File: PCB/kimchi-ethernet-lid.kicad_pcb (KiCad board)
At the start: 4 copper layers, 65 x 32 mm, 8 parts, among them J1 DF40HC(3.5)-60DS, J2 DF40HC(3.5)-60DS, U1 24C32

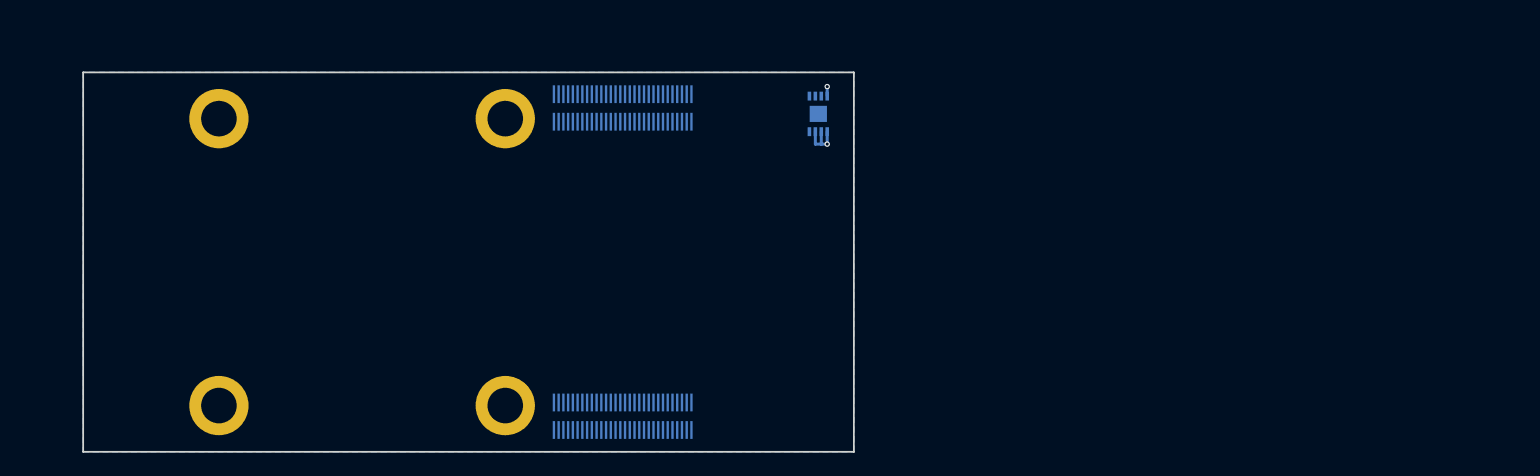
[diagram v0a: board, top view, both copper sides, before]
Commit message: Libraries, Schematic Capture, Part Placement, Lauout
Created and added all realted components. Completed schematic capture. Part placement all bu down, layout in progress since schematic capture.

Had to change out mag jacks a lot to find one that would fit the design
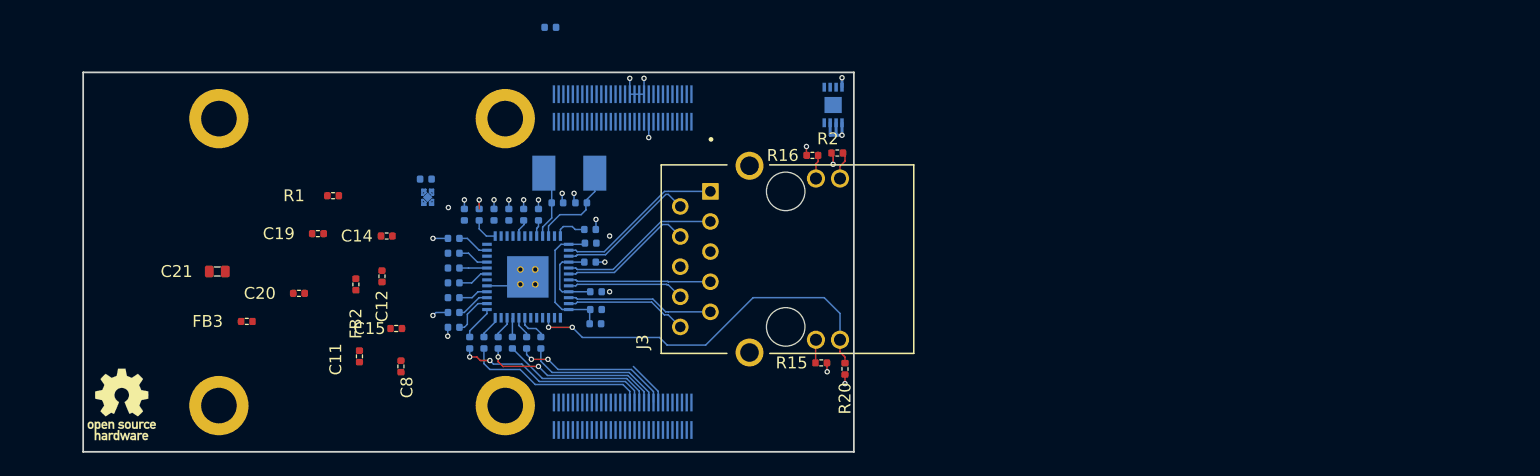
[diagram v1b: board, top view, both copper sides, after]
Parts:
- added C1: C0402C104K9PACTU, AVR-KiCAD-Lib-Resistors:R0402, B.Cu at (150.2, 112.5)
- added C10: C0402C104K9PACTU, AVR-KiCAD-Lib-Resistors:R0402, B.Cu at (142.9, 106.0)
- added C11: C0402C104K9PACTU, AVR-KiCAD-Lib-Resistors:R0402, F.Cu at (130.3, 118.0)
- added C12: C0402C104K9PACTU, AVR-KiCAD-Lib-Resistors:R0402, F.Cu at (132.2, 111.2)
- added C13: C0402C104K9PACTU, AVR-KiCAD-Lib-Resistors:R0402, B.Cu at (138.2, 115.5)
- added C14: C0402C104K9PACTU, AVR-KiCAD-Lib-Resistors:R0402, F.Cu at (132.6, 107.8)
- added C15: 0402ZD105KAT2A, AVR-KiCAD-Lib-Resistors:R0402, F.Cu at (133.4, 115.6)
- added C16: GRM155R61A475MEAAD, kimchi_ulid:C0402, B.Cu at (145.4, 106.0)
- added C17: 04025A180GAT2A, kimchi_ulid:C0402, B.Cu at (149.0, 105.0)
- added C18: 04025A180GAT2A, kimchi_ulid:C0402, B.Cu at (147.0, 105.0)
- added C19: C0402C104K9PACTU, AVR-KiCAD-Lib-Resistors:R0402, F.Cu at (126.8, 107.6)
- added C2: C0402C104K9PACTU, AVR-KiCAD-Lib-Resistors:R0402, B.Cu at (149.8, 110.0)
- added C20: C0402C104K9PACTU, AVR-KiCAD-Lib-Resistors:R0402, F.Cu at (125.2, 112.6)
- added C21: C0603C103KARACAUTO, kimchi_ulid:C0603, F.Cu at (118.3, 110.8)
- added C3: C0402C104K9PACTU, AVR-KiCAD-Lib-Resistors:R0402, B.Cu at (150.2, 114.0)
- added C4: C0402C104K9PACTU, AVR-KiCAD-Lib-Resistors:R0402, B.Cu at (149.8, 108.4)
- added C5: C0402C104K9PACTU, AVR-KiCAD-Lib-Resistors:R0402, B.Cu at (146.4, 90.2)
- added C6: C0402C104K9PACTU, AVR-KiCAD-Lib-Resistors:R0402, B.Cu at (139.2, 106.0)
- added C7: C0402C104K9PACTU, AVR-KiCAD-Lib-Resistors:R0402, B.Cu at (141.7, 106.0)
- added C8: C0402C104K9PACTU, AVR-KiCAD-Lib-Resistors:R0402, F.Cu at (133.8, 118.8)
- added C9: 0402ZD105KAT2A, AVR-KiCAD-Lib-Resistors:R0402, B.Cu at (135.9, 103.0)
- added FB1: MMZ1005S601CTD25, kimchi_ulid:R0402, B.Cu at (150.2, 115.2)
- added FB2: MMZ1005S601CTD25, kimchi_ulid:R0402, F.Cu at (130.0, 111.9)
- added FB3: MMZ1005S601CTD25, kimchi_ulid:R0402, F.Cu at (120.8, 115.0)
- added J3: ARJM11C7-502-AB-ER2-T, kimchi_ulid:ABRACON_ARJM11C7-502-AB-ER2-T, F.Cu at (166.2, 109.8)
- added R1: RC0402FR-071KL, kimchi_ulid:R0402, F.Cu at (128.1, 104.4)
- added R10: RC0402FR-0722RL, kimchi_ulid:R0402, B.Cu at (138.2, 111.8)
- added R11: RC0402FR-0722RL, kimchi_ulid:R0402, B.Cu at (138.2, 113.0)
- added R12: RC0402FR-0722RL, kimchi_ulid:R0402, B.Cu at (138.2, 114.2)
- added R13: RC0402FR-074K7L, kimchi_ulid:R0402, B.Cu at (140.4, 106.0)
- added R15: RC0402FR-071KL, kimchi_ulid:R0402, F.Cu at (169.2, 118.5)
- added R16: RC0402FR-071KL, kimchi_ulid:R0402, F.Cu at (168.5, 101.0)
- added R17: RC0402FR-0710KL, kimchi_ulid:R0402, B.Cu at (144.2, 106.0)
- added R18: RMCF0402FT12K1, kimchi_ulid:R0402, B.Cu at (149.8, 107.2)
- added R2: RC0402FR-071KL, kimchi_ulid:R0402, F.Cu at (170.6, 100.8)
- added R20: RC0402FR-071KL, kimchi_ulid:R0402, F.Cu at (171.2, 119.0)
- added R21: RC0402FR-0722RL, kimchi_ulid:R0402, B.Cu at (140.8, 116.8)
- added R22: RC0402FR-0722RL, kimchi_ulid:R0402, B.Cu at (139.6, 116.8)
- added R23: RC0402FR-0722RL, kimchi_ulid:R0402, B.Cu at (145.6, 116.8)
- added R24: RC0402FR-0722RL, kimchi_ulid:R0402, B.Cu at (144.4, 116.8)
- added R25: RC0402FR-0722RL, kimchi_ulid:R0402, B.Cu at (143.2, 116.8)
- added R26: RC0402FR-0722RL, kimchi_ulid:R0402, B.Cu at (142.0, 116.8)
- added R7: RC0402FR-0722RL, kimchi_ulid:R0402, B.Cu at (138.2, 108.0)
- added R8: RC0402FR-0722RL, kimchi_ulid:R0402, B.Cu at (138.2, 109.2)
- added R9: RC0402FR-0722RL, kimchi_ulid:R0402, B.Cu at (138.2, 110.5)
- added U3: KSZ9031RNXCC, kimchi_ulid:QFN50P700X700X90-49N, B.Cu at (144.5, 111.2)
- added U4: TLV73312PDQNR3, kimchi_ulid:TLV73312PDQNR3, B.Cu at (136.1, 104.5)
- added Y1: ABM3-25.000MHZ-D2Y-T, kimchi_ulid:XTAL500X320X130N, B.Cu at (148.0, 102.5)
- H1, H2, H3, H4: value MountingHole_Pad -> Mechanical_MountingHole_Pad
- LOGO1: value Logo_Open_Hardware_Small -> Graphic_Logo_Open_Hardware_Small; footprint Symbol:OSHW-Logo_5.7x6mm_SilkScreen -> kimchi_ulid:OSHW-Logo_5.7x6mm_SilkScreen; moved to F.Cu
- moved U1 1.46 mm to (170.2, 96.8)
- moved LOGO1 1.25 mm to (110.2, 122.0), turned to 0 degrees
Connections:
- J1 pad 1: (no net) -> /USDHC3_CMD
- J1 pad 17: (no net) -> I2C3_SDA
- J1 pad 18: (no net) -> I2C3_SCL
- J1 pad 19: (no net) -> I2C2_SDA
- J1 pad 2: (no net) -> /USDHC3_CLK
- J1 pad 20: (no net) -> I2C2_SCL
- J1 pad 21: (no net) -> I2C1_SDA
- J1 pad 22: (no net) -> I2C1_SCL
- J1 pad 23: (no net) -> ECSPI1_SCLK
- J1 pad 24: (no net) -> ECSPI1_SS0
- J1 pad 25: (no net) -> ECSPI1_MOSI
- J1 pad 26: (no net) -> ECSPI1_MISO
- J1 pad 27: (no net) -> ECSPI2_SCLK
- J1 pad 28: (no net) -> ECSPI2_SS0
- J1 pad 29: (no net) -> ECSPI2_MOSI
- J1 pad 3: (no net) -> /USDHC3_DATA3
- J1 pad 30: (no net) -> ECSPI2_MISO
- J1 pad 31: (no net) -> /DISP_D0_N
- J1 pad 32: (no net) -> /DISP_D0_P
- J1 pad 33: (no net) -> /DISP_D1_N
- J1 pad 34: (no net) -> /DISP_D1_P
- J1 pad 35: (no net) -> /DISP_CK_N
- J1 pad 36: (no net) -> /DISP_CK_P
- J1 pad 37: (no net) -> /DISP_D2_N
- J1 pad 38: (no net) -> /DISP_D2_P
- J1 pad 39: (no net) -> /DISP_D3_N
- J1 pad 4: (no net) -> /USDHC3_DATA0
- J1 pad 40: (no net) -> /DISP_D3_P
- J1 pad 41: (no net) -> /CAM_D0_N
- J1 pad 42: (no net) -> /CAM_D0_P
- J1 pad 43: (no net) -> /CAM_D1_N
- J1 pad 44: (no net) -> /CAM_D1_P
- J1 pad 45: (no net) -> /CAM_CK_N
- J1 pad 46: (no net) -> /CAM_CK_P
- J1 pad 47: (no net) -> /CAM_D2_N
- J1 pad 48: (no net) -> /CAM_D2_P
- J1 pad 49: (no net) -> /CAM_D3_N
- J1 pad 5: (no net) -> /USDHC3_DATA1
- J1 pad 50: (no net) -> /CAM_D3_P
- J1 pad 52: (no net) -> UIM_VPP
- J1 pad 53: (no net) -> UIM_RESET_N
- J1 pad 54: (no net) -> UIM_CLK
- J1 pad 55: (no net) -> UIM_DATA
- J1 pad 56: (no net) -> UIM_PWR
- J1 pad 57: (no net) -> USB2_VBUS
- J1 pad 58: (no net) -> USB2_ID
- J1 pad 59: (no net) -> USB2_DN
- J1 pad 6: (no net) -> /USDHC3_DATA2
- J1 pad 60: (no net) -> USB2_DP
- J2 pad 1: (no net) -> /ENET_MDIO
- J2 pad 10: (no net) -> /ENET_TD0
- J2 pad 11: (no net) -> /ENET_TD3
- J2 pad 12: (no net) -> /ENET_TD2
- J2 pad 13: (no net) -> /ENET_TX_CTL
- J2 pad 14: (no net) -> /ENET_TXC
- J2 pad 15: (no net) -> SAI2_RXD0
- J2 pad 16: (no net) -> SAI2_TXFS
- J2 pad 17: (no net) -> SAI2_RXC
- J2 pad 18: (no net) -> SAI2_TXD0
- J2 pad 19: (no net) -> SAI2_TXC
- J2 pad 2: (no net) -> /ENET_MDC
- J2 pad 20: (no net) -> SAI2_MCLK
- J2 pad 21: (no net) -> SAI2_RXFS
- J2 pad 22: (no net) -> GPIO1[15]
- J2 pad 23: (no net) -> GPIO1[14]
- J2 pad 24: (no net) -> GPIO1[13]
- J2 pad 25: (no net) -> GPIO1[12]
- J2 pad 26: (no net) -> GPIO1[11]
- J2 pad 27: (no net) -> GPIO1[10]
- J2 pad 28: (no net) -> GPIO1[9]
- J2 pad 29: (no net) -> GPIO1[1]
- J2 pad 3: (no net) -> /ENET_RD3
- J2 pad 30: (no net) -> GPIO1[0]
- J2 pad 31: (no net) -> SAI3_TXC
- J2 pad 32: (no net) -> SAI3_TXD
- J2 pad 33: (no net) -> SAI3_RXD
- J2 pad 34: (no net) -> SAI3_RXFS
- J2 pad 35: (no net) -> SAI3_RXC
- J2 pad 36: (no net) -> SAI3_TXFS
- J2 pad 37: (no net) -> SAI3_MCLK
- J2 pad 4: (no net) -> /ENET_RD1
- J2 pad 46: (no net) -> UART1_TX
- J2 pad 47: (no net) -> UART1_RX
- J2 pad 48: (no net) -> UART3_TX
- J2 pad 49: (no net) -> UART3_RX
- J2 pad 5: (no net) -> /ENET_RD2
- J2 pad 58: (no net) -> Net-(J2-Pad58)
- J2 pad 59: (no net) -> PCIE_USB_D_P
- J2 pad 6: (no net) -> /ENET_RD0
- J2 pad 60: (no net) -> PCIE_USB_D_N
- J2 pad 7: (no net) -> /ENET_RXC
- J2 pad 8: (no net) -> /ENET_RX_CTL
- J2 pad 9: (no net) -> /ENET_TD1
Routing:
- net /LED2: track 0.00 -> 32.6 mm, vias 0 -> 2
- net GND: track 0.00 -> 17.8 mm, vias 0 -> 16
- net /ENET_TX_CTL: track 0.00 -> 16.8 mm, vias 0 -> 2
- net /ENET_TXC: track 0.00 -> 15.5 mm
- net /ENET_TD3: track 0.00 -> 15.4 mm, vias 0 -> 2
- net /TRD1+: track 0.00 -> 14.1 mm
- net /TRD2+: track 0.00 -> 13.7 mm
- net /ENET_TD1: track 0.00 -> 13.4 mm, vias 0 -> 2
- net /ENET_TD2: track 0.00 -> 13.1 mm
- net /TRD4+: track 0.00 -> 12.4 mm
- net /ENET_TD0: track 0.00 -> 12.1 mm
- net /TRD3+: track 0.00 -> 12.0 mm
- net /TRD1-: track 0.00 -> 12.0 mm
- net Net-(C3-Pad1): track 0.00 -> 11.6 mm
- net /TRD2-: track 0.00 -> 11.6 mm
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- added copper zone on In2.Cu, net VDD_PHY_1V2
- removed copper zone on B.Cu, net GND
- removed copper zone on In2.Cu, net VDD_3V3

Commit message: Change in design
Swapped orientation of PHY and position of ethernet connector, moving computers
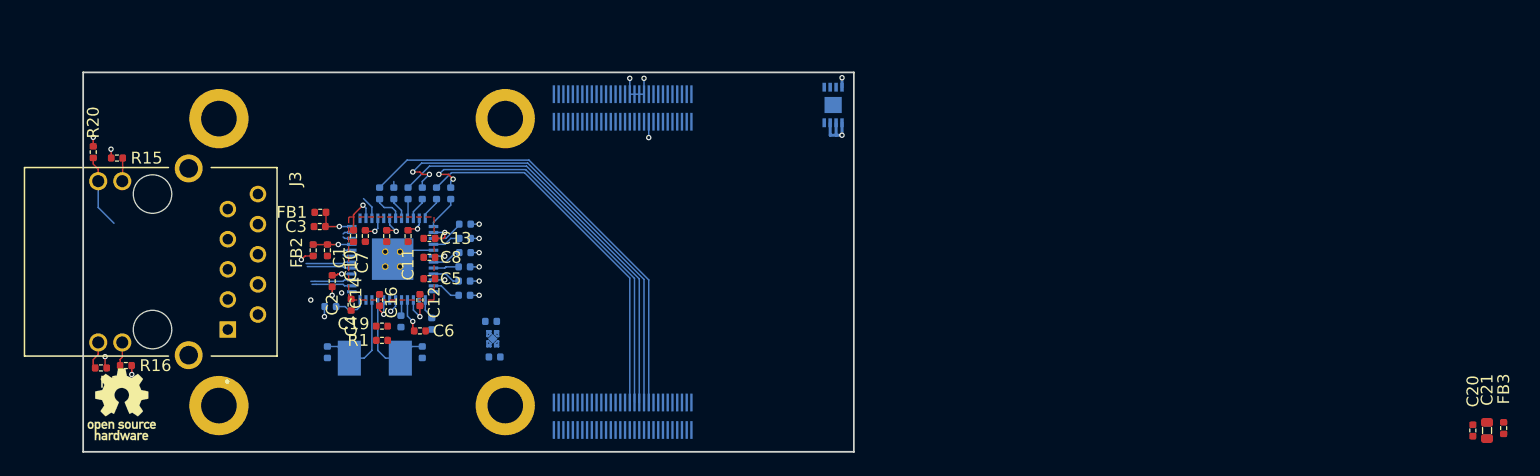
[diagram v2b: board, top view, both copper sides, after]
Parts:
- C1, C10, C13, C16, C2, C3, C4, C5, C6, C7, FB1: moved to F.Cu
- C15: moved to B.Cu
- moved C21 107.9 mm to (225.4, 124.2), turned to 270 degrees
- moved FB3 106.4 mm to (226.8, 124.0), turned to 270 degrees
- moved C20 99.7 mm to (224.2, 124.2), turned to 270 degrees
- moved R20 66.0 mm to (107.8, 100.7), turned to 90 degrees
- moved R2 64.7 mm to (108.5, 118.9), turned to 180 degrees
- moved R15 61.9 mm to (109.8, 101.2), turned to 0 degrees
- moved R16 60.6 mm to (110.6, 118.7), turned to 180 degrees
- moved J3 53.4 mm to (112.8, 110.0), turned to 270 degrees
- moved FB1 25.0 mm to (127.0, 105.8), turned to 180 degrees
- moved C17 24.8 mm to (127.6, 117.6), turned to 270 degrees
- moved C3 24.3 mm to (127.0, 107.0), turned to 180 degrees
- moved C5 23.5 mm to (136.2, 111.4), turned to 180 degrees
- moved C1 22.9 mm to (127.6, 109.0), turned to 270 degrees
- moved R18 22.8 mm to (127.8, 113.8), turned to 0 degrees
- moved Y1 22.6 mm to (131.6, 118.1), turned to 0 degrees
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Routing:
- net /ENET_TD0: track 12.1 -> 38.2 mm
- net /LED2: track 32.6 -> 8.19 mm, vias 2 -> 0
- net /ENET_TD3: track 15.4 -> 37.1 mm
- net /ENET_TD2: track 13.1 -> 34.6 mm
- net /ENET_TX_CTL: track 16.8 -> 33.1 mm
- net /ENET_TXC: track 15.5 -> 31.0 mm
- net /ENET_TD1: track 13.4 -> 0.52 mm, vias 2 -> 0
- net /TRD4+: track 12.4 -> 0.78 mm
- net /TRD3+: track 12.0 -> 0.78 mm
- net VDD_PHY_1V2: track 3.65 -> 14.5 mm, vias 0 -> 7
- net /TRD1+: track 14.1 -> 3.40 mm
- net /TRD2+: track 13.7 -> 3.80 mm
- net /TRD4-: track 10.3 -> 0.78 mm
- net /TRD3-: track 9.90 -> 0.78 mm
- net /TRD1-: track 12.0 -> 3.51 mm
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- added copper zone on F.Cu, net GND

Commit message: Route Complete
RMGII signals routed to kimchi headers, ENET diff pairs tuned routed to connector. Power distribution scheme designed and implemented. First pass of route done, Further analysis need for RGMII interface trace length tuning
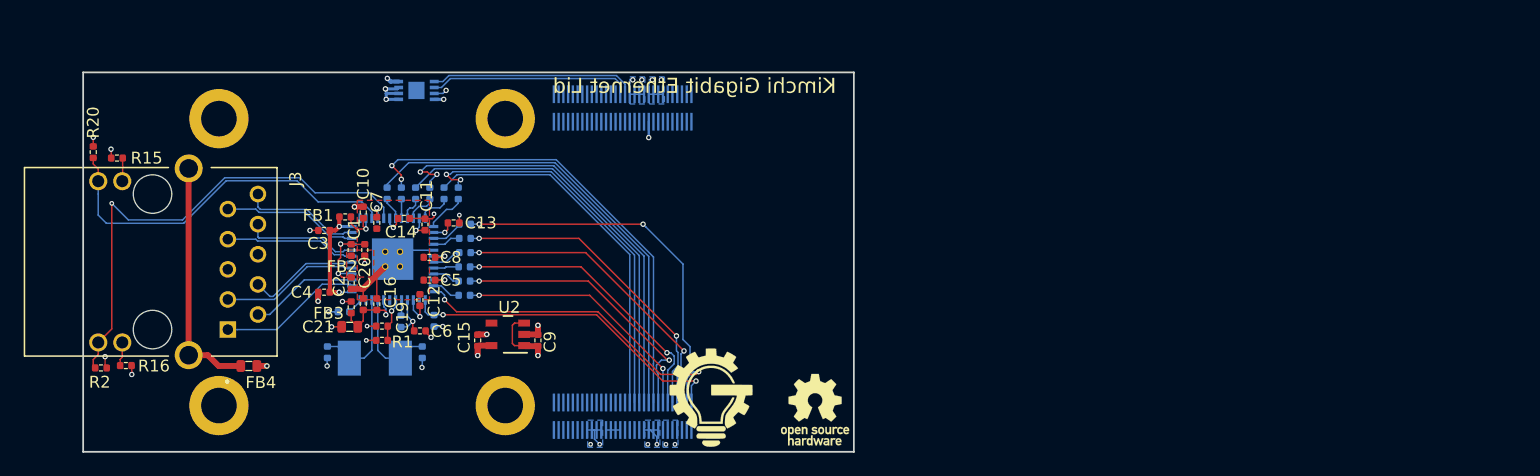
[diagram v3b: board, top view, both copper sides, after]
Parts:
- removed U4: TLV73312PDQNR3, kimchi_ulid:TLV73312PDQNR3
- added FB4: FBMJ1608HM180NTR, kimchi_ulid:R0603, F.Cu at (121.0, 118.8)
- added L1: GG_LOGO, kimchi_ulid:groupgets_logo, F.Cu at (160.0, 121.4)
- added U2: TLV75712PDBVR, kimchi_ulid:TLV75712PDBVR, F.Cu at (142.8, 116.1)
- C15, C9: moved to F.Cu
- moved FB3 97.7 mm to (129.6, 113.8), turned to 90 degrees
- moved C21 96.3 mm to (129.5, 115.5), turned to 180 degrees
- moved C20 94.2 mm to (130.6, 113.6), turned to 90 degrees
- moved LOGO1 58.5 mm to (168.7, 122.4)
- moved U1 35.2 mm to (135.1, 95.5), turned to 0 degrees
- moved FB2 4.35 mm to (130.7, 109.0)
- moved C9 3.91 mm to (145.4, 116.6), turned to 90 degrees
- moved C4 2.52 mm to (127.3, 112.5), turned to 180 degrees
- moved C13 2.42 mm to (138.2, 106.7), turned to 0 degrees
- moved C10 2.16 mm to (130.6, 105.8), turned to 90 degrees
- moved FB1 2.13 mm to (129.1, 106.2), turned to 0 degrees
- moved C14 2.08 mm to (134.1, 106.3), turned to 0 degrees
- moved C1 2.01 mm to (129.6, 109.0)
- moved C15 1.96 mm to (140.3, 116.6), turned to 90 degrees
- moved C11 1.73 mm to (135.8, 106.8), turned to 90 degrees
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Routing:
- net /ENET_TD1: track 0.52 -> 40.1 mm, vias 0 -> 2
- net /LED1: track 2.13 -> 41.3 mm, vias 0 -> 1
- net /ENET_RD3: track 0.72 -> 31.5 mm, vias 1 -> 2
- net /ENET_MDC: track 0.00 -> 28.9 mm, vias 0 -> 2
- net VDD_PHY_1V2: track 14.5 -> 42.8 mm, vias 7 -> 9
- net /ENET_MDIO: track 1.75 -> 28.3 mm, vias 0 -> 2
- net /ENET_RD2: track 0.72 -> 26.6 mm, vias 1 -> 2
- net /ENET_RD1: track 0.72 -> 26.0 mm, vias 1 -> 2
- net GND: track 12.2 -> 36.1 mm, vias 7 -> 24
- net /ENET_RD0: track 0.77 -> 24.5 mm, vias 1 -> 2
- net /LED2: track 8.19 -> 31.5 mm
- net /ENET_RX_CTL: track 0.77 -> 24.0 mm, vias 1 -> 2
- net /ENET_RXC: track 0.77 -> 21.7 mm, vias 1 -> 2
- net Net-(FB4-Pad1): track 0.00 -> 20.5 mm
- net I2C4_SDA: track 0.00 -> 17.5 mm
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- added copper zone on B.Cu, net GND
- added copper zone on B.Cu, net VDD_3V3
- added copper zone on In2.Cu, net VDD_3V3
- added copper zone on B.Cu, net VDD_5V
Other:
- board text added: "Kimchi Gigabit Ethernet Lid"

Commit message: Memory Module
Memory module moved, USB to PCIe passthrough added. BOM created in libreoffice format, CSV from component fields also generated.
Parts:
- moved U1 34.7 mm to (169.7, 98.1), turned to 90 degrees
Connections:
- J2 pad 59: PCIE_USB_D_P -> USB2_DN
- J2 pad 60: PCIE_USB_D_N -> USB2_DP
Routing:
- net USB2_DN: track 0.00 -> 27.6 mm
- net USB2_DP: track 0.00 -> 27.4 mm
- net I2C4_SCL: track 17.1 -> 19.9 mm, vias 0 -> 2
- net I2C4_SDA: track 17.5 -> 18.8 mm, vias 0 -> 2

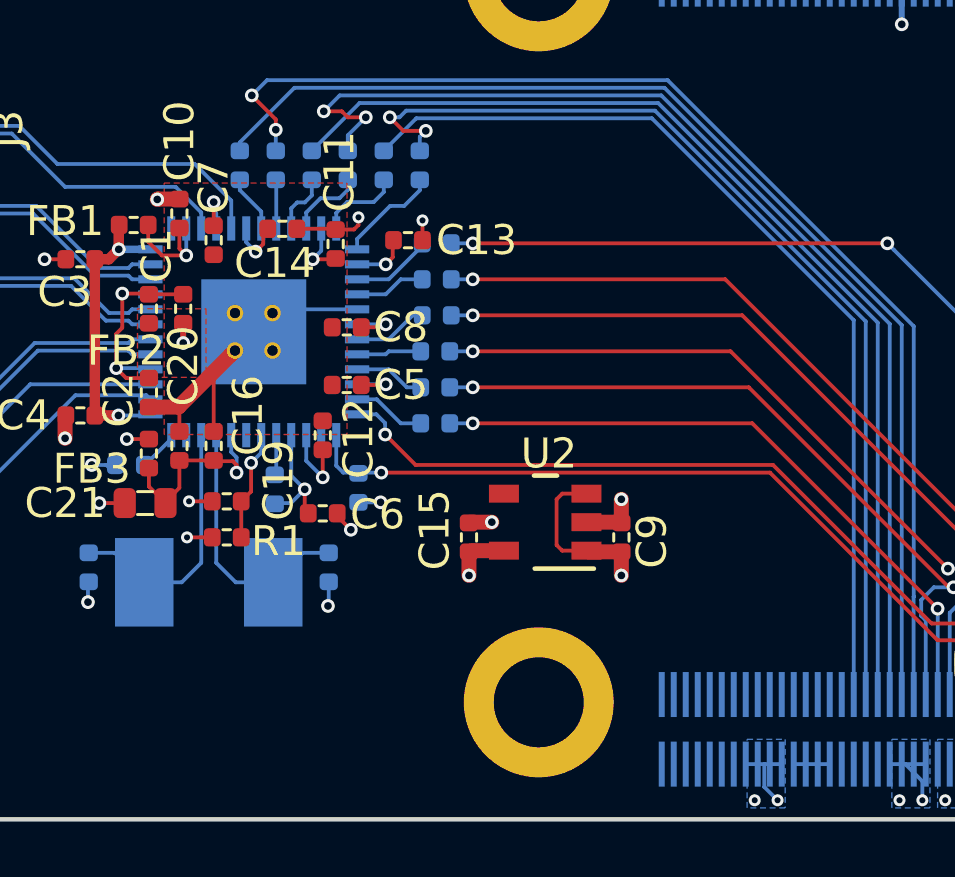
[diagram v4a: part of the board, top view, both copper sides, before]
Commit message: Pullups
Pullup resistors added to RGMII interface setup on boot.
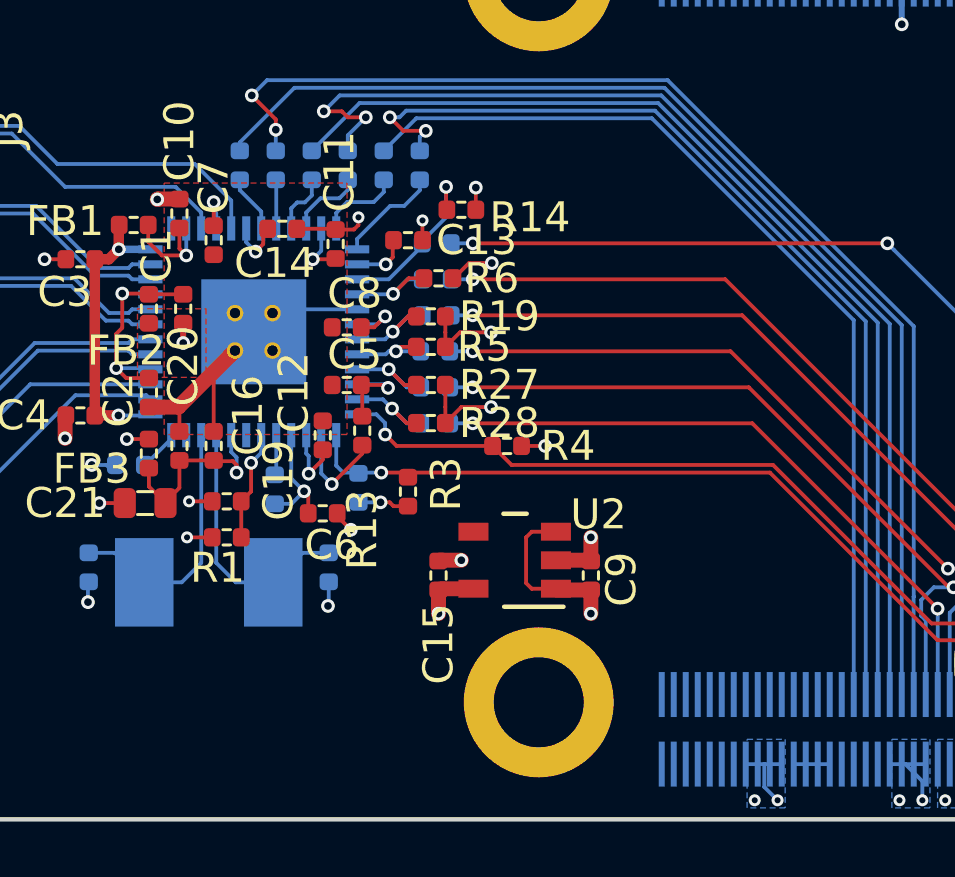
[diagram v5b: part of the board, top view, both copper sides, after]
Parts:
- added R13: RC0402FR-0710KL, kimchi_ulid:R0402, F.Cu at (136.7, 113.0)
- added R14: RC0402FR-0710KL, kimchi_ulid:R0402, F.Cu at (140.0, 105.7)
- added R19: RC0402FR-0710KL, kimchi_ulid:R0402, F.Cu at (139.0, 109.2)
- added R27: RC0402FR-071KL, kimchi_ulid:R0402, F.Cu at (139.0, 111.5)
- added R28: RC0402FR-071KL, kimchi_ulid:R0402, F.Cu at (139.0, 112.8)
- added R3: RC0402FR-071KL, kimchi_ulid:R0402, F.Cu at (138.2, 115.1)
- added R4: RC0402FR-071KL, kimchi_ulid:R0402, F.Cu at (141.5, 113.6)
- added R5: RC0402FR-0710KL, kimchi_ulid:R0402, F.Cu at (139.0, 110.3)
- added R6: RC0402FR-0710KL, kimchi_ulid:R0402, F.Cu at (139.3, 108.0)
- moved C9 1.63 mm to (144.3, 117.9)
- moved U2 1.63 mm to (141.8, 117.4)
- moved C15 1.63 mm to (139.3, 117.9)
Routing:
- net VDD_3V3: track 22.1 -> 30.1 mm, vias 14 -> 18
- net Net-(R13-Pad1): track 0.00 -> 3.49 mm, vias 0 -> 1
- net GND: track 36.2 -> 39.2 mm, vias 24 -> 25
- net Net-(R12-Pad1): track 2.72 -> 5.70 mm, vias 0 -> 1
- net Net-(R11-Pad1): track 2.38 -> 3.62 mm, vias 0 -> 1
- net Net-(R27-Pad1): track 2.37 -> 3.51 mm, vias 0 -> 1
- net Net-(R28-Pad1): track 2.52 -> 3.53 mm, vias 0 -> 1
- net Net-(R10-Pad1): track 2.59 -> 3.58 mm, vias 0 -> 1
- net Net-(R5-Pad1): track 2.16 -> 2.91 mm, vias 0 -> 1
